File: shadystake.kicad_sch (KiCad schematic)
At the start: 19 parts, among them J1 6P6C, J2 6P6C, J3 6P6C, J4 6P6C, J5 6P6C, J6 6P6C, J7 8P8C

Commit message: More updates
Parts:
- added TP1, TP2, TP3, TP4, TP5, TP6, TP7, TP8: TestPoint, Shadystake:TP, symbol Connector:TestPoint
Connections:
- net RING1: now also TP2.1
- net RING2: now also TP4.1
- net RING3: now also TP6.1
- net RING4: now also TP8.1
- net TIP1: now also TP1.1
- net TIP2: now also TP3.1
- net TIP3: now also TP5.1
- net TIP4: now also TP7.1
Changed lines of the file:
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@@
     (pin "2")
+  )
+  (symbol (lib_id "Connector:TestPoint") (at 133.35 72.39 0) (unit 1)
+    (in_bom yes) (on_board yes)
+    (property "Reference" "TP1" (id 0) (at 135.89 69.0879 0)
+      (effects (font (size 1.27 1.27)) (justify left))
+    )
+    (property "Value" "TestPoint" (id 1) (at 135.89 70.3579 0)
+      (effects (font (size 1.27 1.27)) (justify left) hide)
+    )
+    (property "Footprint" "Shadystake:TP" (id 2) (at 138.43 72.39 0)
+      (effects (font (size 1.27 1.27)) hide)
+    )
+    (property "Datasheet" "~" (id 3) (at 138.43 72.39 0)
+      (effects (font (size 1.27 1.27)) hide)
+    )
+    (pin "1")
   )
   (symbol (lib_id "shadystake-rescue:SPARK_GAP-Device") (at 184.15 80.01 0) (mirror x) (unit 1)
@@
     (pin "2")
   )
+  (symbol (lib_id "Connector:TestPoint") (at 190.5 72.39 0) (unit 1)
+    (in_bom yes) (on_board yes) (fields_autoplaced)
+    (property "Reference" "TP6" (id 0) (at 193.04 69.0879 0)
+      (effects (font (size 1.27 1.27)) (justify left))
+    )
+    (property "Value" "TestPoint" (id 1) (at 193.04 70.3579 0)
+      (effects (font (size 1.27 1.27)) (justify left) hide)
+    )
+    (property "Footprint" "Shadystake:TP" (id 2) (at 195.58 72.39 0)
+      (effects (font (size 1.27 1.27)) hide)
+    )
+    (property "Datasheet" "~" (id 3) (at 195.58 72.39 0)
+      (effects (font (size 1.27 1.27)) hide)
+    )
+    (pin "1")
+  )
+  (symbol (lib_id "Connector:TestPoint") (at 212.09 72.39 0) (unit 1)
+    (in_bom yes) (on_board yes) (fields_autoplaced)
+    (property "Reference" "TP8" (id 0) (at 214.63 69.0879 0)
+      (effects (font (size 1.27 1.27)) (justify left))
+    )
+    (property "Value" "TestPoint" (id 1) (at 214.63 70.3579 0)
+      (effects (font (size 1.27 1.27)) (justify left) hide)
+    )
+    (property "Footprint" "Shadystake:TP" (id 2) (at 217.17 72.39 0)
+      (effects (font (size 1.27 1.27)) hide)
+    )
+    (property "Datasheet" "~" (id 3) (at 217.17 72.39 0)
+      (effects (font (size 1.27 1.27)) hide)
+    )
+    (pin "1")
+  )
   (symbol (lib_id "shadystake-rescue:SPARK_GAP-Device") (at 205.74 80.01 180) (unit 1)
     (in_bom yes) (on_board yes)
@@
     (pin "1")
     (pin "2")
+  )
+  (symbol (lib_id "Connector:TestPoint") (at 199.39 72.39 0) (unit 1)
+    (in_bom yes) (on_board yes) (fields_autoplaced)
+    (property "Reference" "TP7" (id 0) (at 201.93 69.0879 0)
+      (effects (font (size 1.27 1.27)) (justify left))
+    )
+    (property "Value" "TestPoint" (id 1) (at 201.93 70.3579 0)
+      (effects (font (size 1.27 1.27)) (justify left) hide)
+    )
+    (property "Footprint" "Shadystake:TP" (id 2) (at 204.47 72.39 0)
+      (effects (font (size 1.27 1.27)) hide)
+    )
+    (property "Datasheet" "~" (id 3) (at 204.47 72.39 0)
+      (effects (font (size 1.27 1.27)) hide)
+    )
+    (pin "1")
+  )
+  (symbol (lib_id "Connector:TestPoint") (at 167.64 72.39 0) (unit 1)
+    (in_bom yes) (on_board yes) (fields_autoplaced)
+    (property "Reference" "TP4" (id 0) (at 170.18 69.0879 0)
+      (effects (font (size 1.27 1.27)) (justify left))
+    )
+    (property "Value" "TestPoint" (id 1) (at 170.18 70.3579 0)
+      (effects (font (size 1.27 1.27)) (justify left) hide)
+    )
+    (property "Footprint" "Shadystake:TP" (id 2) (at 172.72 72.39 0)
+      (effects (font (size 1.27 1.27)) hide)
+    )
+    (property "Datasheet" "~" (id 3) (at 172.72 72.39 0)
+      (effects (font (size 1.27 1.27)) hide)
+    )
+    (pin "1")
   )
   (symbol (lib_id "shadystake-rescue:6P6C-Connector") (at 92.71 121.92 0) (unit 1)
@@
     (pin "6")
   )
+  (symbol (lib_id "Connector:TestPoint") (at 146.05 72.39 0) (unit 1)
+    (in_bom yes) (on_board yes) (fields_autoplaced)
+    (property "Reference" "TP2" (id 0) (at 148.59 69.0879 0)
+      (effects (font (size 1.27 1.27)) (justify left))
+    )
+    (property "Value" "TestPoint" (id 1) (at 148.59 70.3579 0)
+      (effects (font (size 1.27 1.27)) (justify left) hide)
+    )
+    (property "Footprint" "Shadystake:TP" (id 2) (at 151.13 72.39 0)
+      (effects (font (size 1.27 1.27)) hide)
+    )
+    (property "Datasheet" "~" (id 3) (at 151.13 72.39 0)
+      (effects (font (size 1.27 1.27)) hide)
+    )
+    (pin "1")
+  )
   (symbol (lib_id "shadystake-rescue:SPARK_GAP-Device") (at 139.7 80.01 180) (unit 1)
     (in_bom yes) (on_board yes)
@@
     (pin "2")
   )
+  (symbol (lib_id "Connector:TestPoint") (at 154.94 72.39 0) (unit 1)
+    (in_bom yes) (on_board yes) (fields_autoplaced)
+    (property "Reference" "TP3" (id 0) (at 157.48 69.0879 0)
+      (effects (font (size 1.27 1.27)) (justify left))
+    )
+    (property "Value" "TestPoint" (id 1) (at 157.48 70.3579 0)
+      (effects (font (size 1.27 1.27)) (justify left) hide)
+    )
+    (property "Footprint" "Shadystake:TP" (id 2) (at 160.02 72.39 0)
+      (effects (font (size 1.27 1.27)) hide)
+    )
+    (property "Datasheet" "~" (id 3) (at 160.02 72.39 0)
+      (effects (font (size 1.27 1.27)) hide)
+    )
+    (pin "1")
+  )
   (symbol (lib_id "power:PWR_FLAG") (at 171.45 100.33 90) (unit 1)
     (in_bom yes) (on_board yes) (fields_autoplaced)
@@
     )
     (property "Datasheet" "~" (id 3) (at 171.45 100.33 0)
+      (effects (font (size 1.27 1.27)) hide)
+    )
+    (pin "1")
+  )
+  (symbol (lib_id "Connector:TestPoint") (at 177.8 72.39 0) (unit 1)
+    (in_bom yes) (on_board yes) (fields_autoplaced)
+    (property "Reference" "TP5" (id 0) (at 180.34 69.0879 0)
+      (effects (font (size 1.27 1.27)) (justify left))
+    )
+    (property "Value" "TestPoint" (id 1) (at 180.34 70.3579 0)
+      (effects (font (size 1.27 1.27)) (justify left) hide)
+    )
+    (property "Footprint" "Shadystake:TP" (id 2) (at 182.88 72.39 0)
+      (effects (font (size 1.27 1.27)) hide)
+    )
+    (property "Datasheet" "~" (id 3) (at 182.88 72.39 0)
       (effects (font (size 1.27 1.27)) hide)
     )
@@
       (reference "J7") (unit 1) (value "8P8C") (footprint "Shadystake:8P8C_Hor")
     )
-  )
+    (path "/0a098971-8170-4313-af7d-cc4b35a48563"
+      (reference "TP1") (unit 1) (value "TestPoint") (footprint "Shadystake:TP")
+    )
+    (path "/852d7eb3-be75-4a91-a77c-983a0b48cb78"
+      (reference "TP2") (unit 1) (value "TestPoint") (footprint "Shadystake:TP")
+    )
+    (path "/acce9e8d-1af5-4185-9b26-f4e12168abf6"
+      (reference "TP3") (unit 1) (value "TestPoint") (footprint "Shadystake:TP")
+    )
+    (path "/3a9d0b00-96d7-4fd0-bdc5-d104420acca5"
+      (reference "TP4") (unit 1) (value "TestPoint") (footprint "Shadystake:TP")
+    )
+    (path "/e21fac56-b274-477f-b454-6d91d51c7236"
+      (reference "TP5") (unit 1) (value "TestPoint") (footprint "Shadystake:TP")
+    )
+    (path "/16866a64-c8d3-4fa6-87e7-e15e690191a6"
+      (reference "TP6") (unit 1) (value "TestPoint") (footprint "Shadystake:TP")
+    )
+    (path "/3190d7e0-a61f-4ca4-b327-9b533cabbe43"
+      (reference "TP7") (unit 1) (value "TestPoint") (footprint "Shadystake:TP")
+    )
+    (path "/1d3ea86f-e865-473d-82a1-7f4a62523f60"
+      (reference "TP8") (unit 1) (value "TestPoint") (footprint "Shadystake:TP")
+    )
+  )

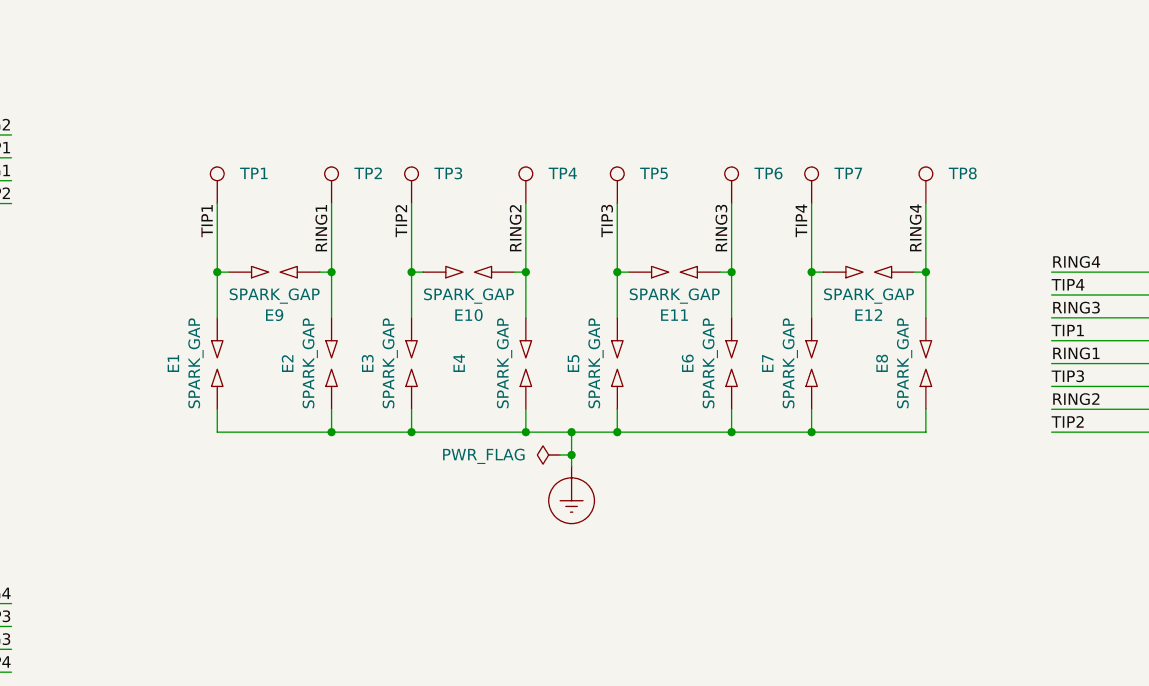
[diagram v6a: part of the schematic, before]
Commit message: Remove circuit protection
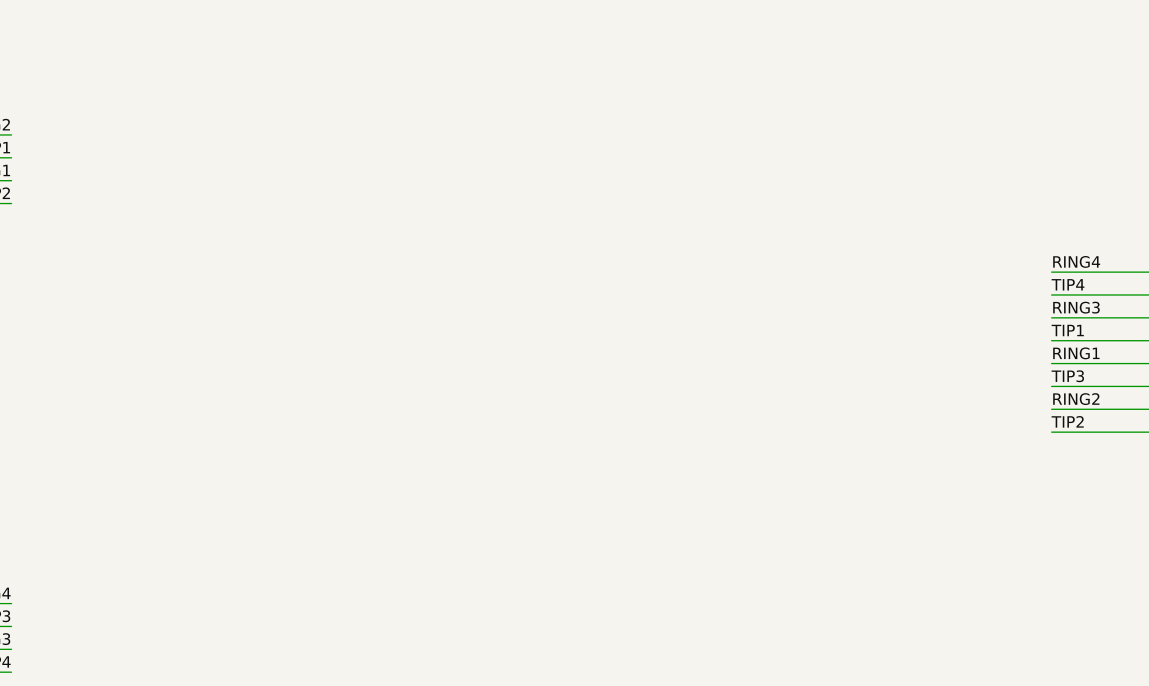
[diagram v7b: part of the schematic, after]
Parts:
- removed E1, E10, E11, E12, E2, E3, E4, E5, E6, E7, E8, E9: SPARK_GAP, Shadystake:Spark_Gap_Teeth, symbol shadystake-rescue:SPARK_GAP-Device
- removed TP1, TP2, TP3, TP4, TP5, TP6, TP7, TP8: TestPoint, Shadystake:TP, symbol Connector:TestPoint
